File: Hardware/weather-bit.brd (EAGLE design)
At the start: 68.6 x 67.3 mm, 42 parts, among them J2 RJ11, J3 RJ11, U1 BME280, U2 micro:bit

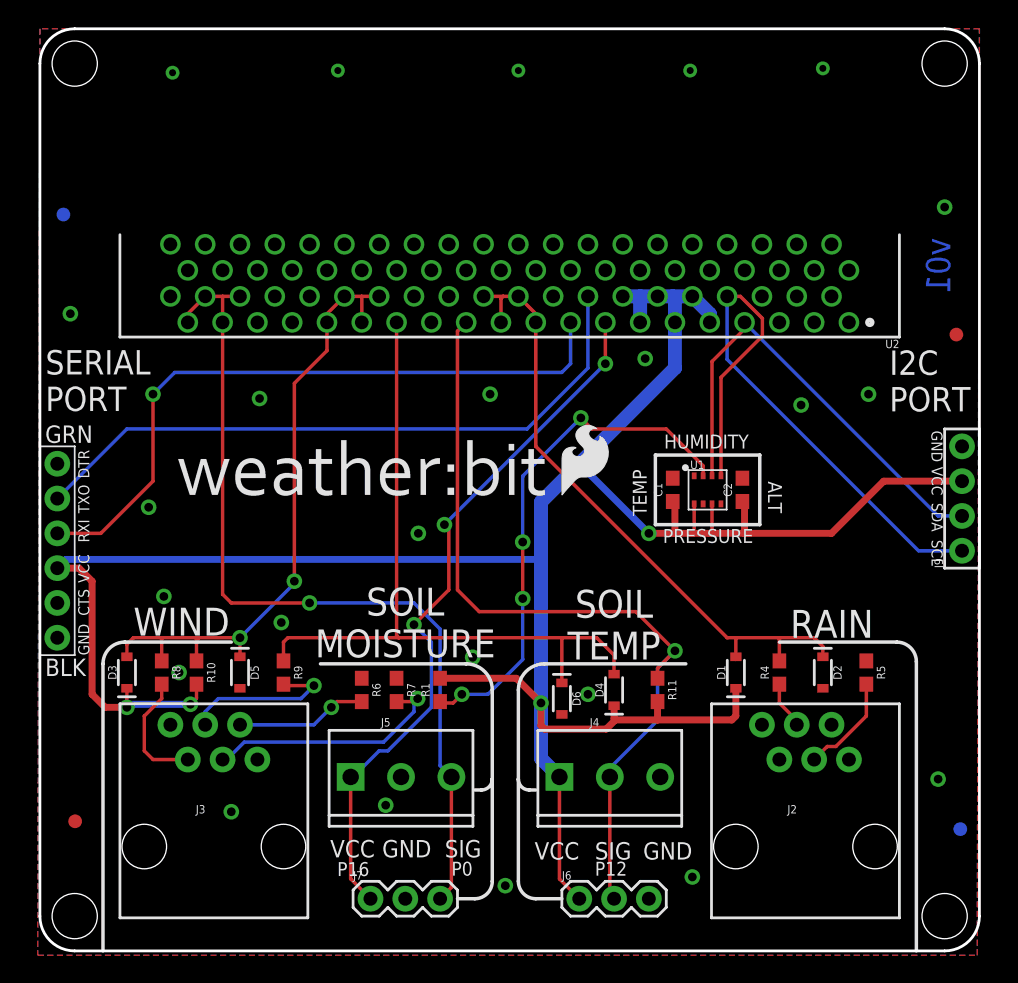
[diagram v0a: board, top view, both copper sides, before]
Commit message: Updated One-Wire Hardware Set-up
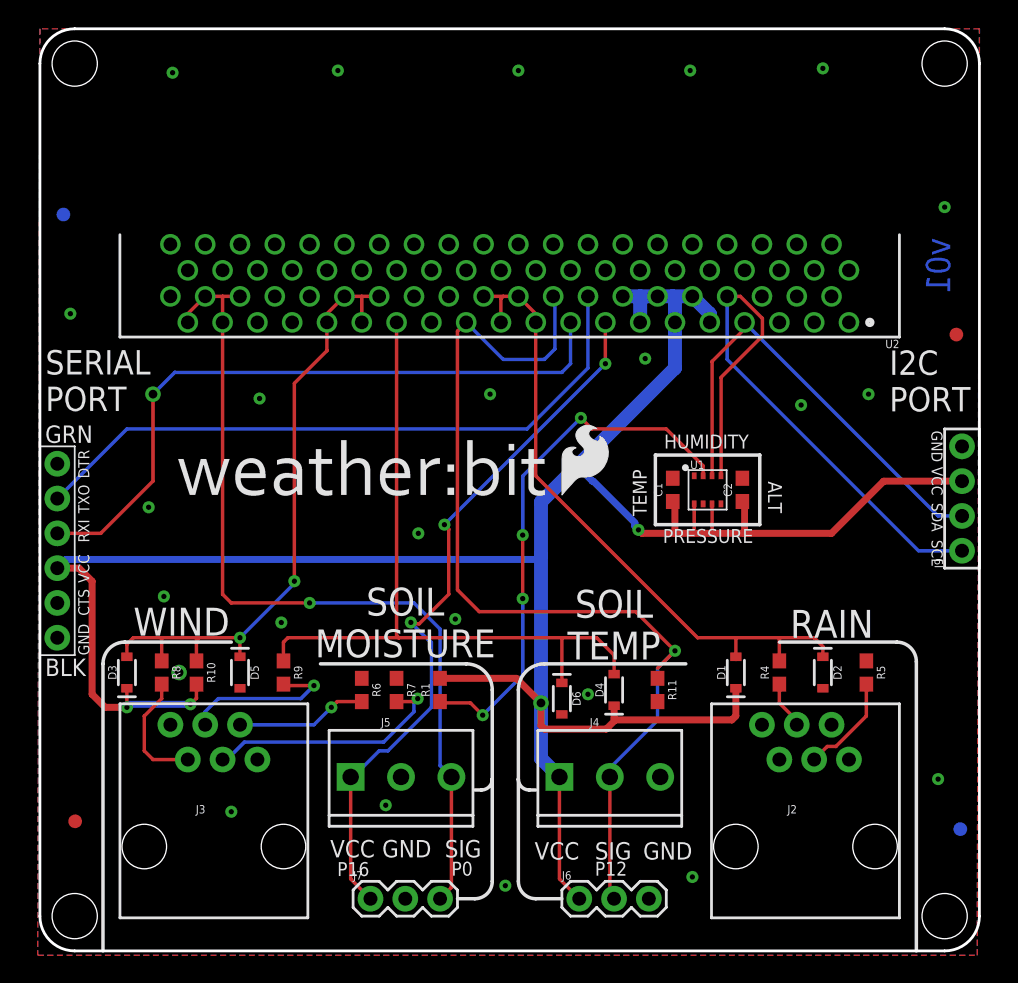
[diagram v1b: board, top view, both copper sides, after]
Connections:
- removed net 13: U2.A18
- net 3.3V: now also R11.1; no longer R11.2
- net TEMP_DAT: now also R11.2, U2.A18; no longer R11.1
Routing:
- net TEMP_DAT: track 60.2 -> 71.4 mm
- net N$2: track 37.9 -> 39.4 mm
- net RAIN: track 47.0 -> 48.3 mm
- net 3.3V: track 186.1 -> 184.9 mm
- net SOIL_PWR: track 52.2 -> 52.9 mm

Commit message: Updating weather:bit per QC review
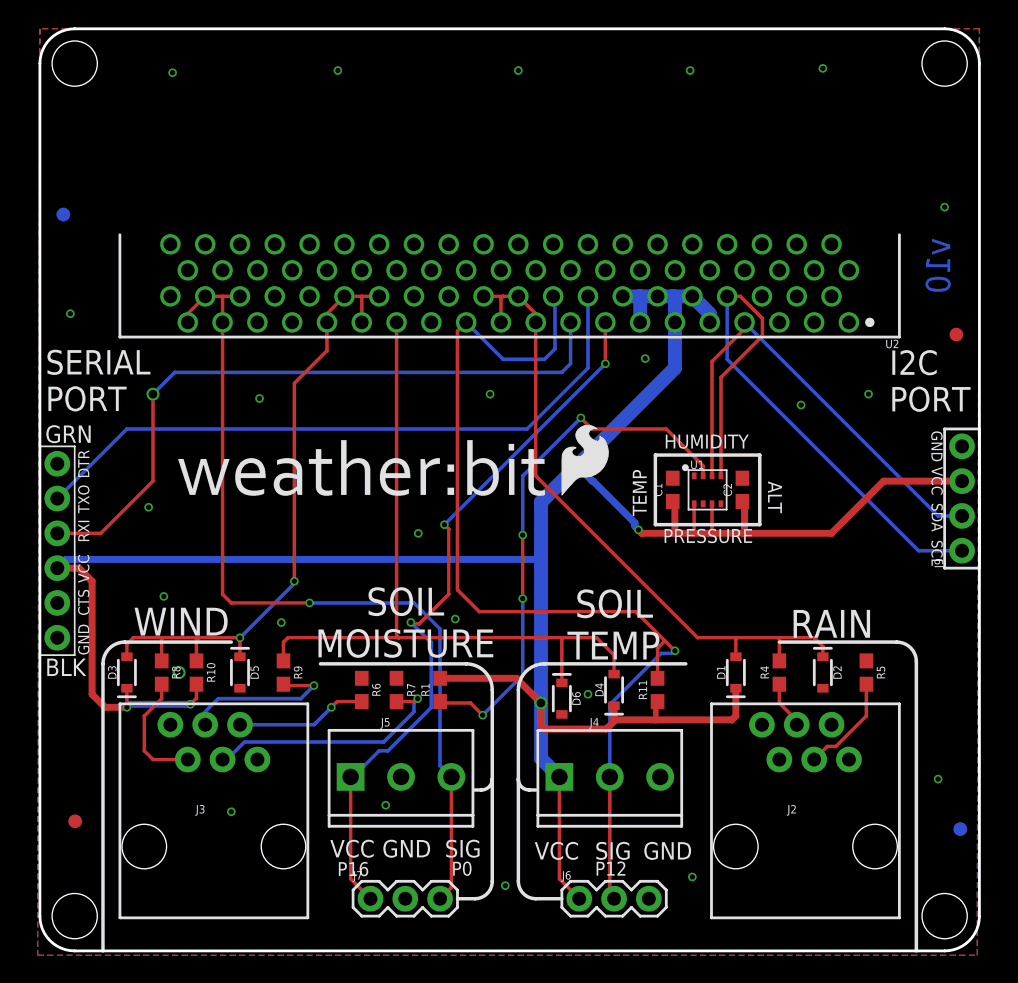
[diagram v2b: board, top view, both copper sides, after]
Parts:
- added U$4: (no value), SparkFun-Aesthetics:ORDERING_INSTRUCTIONS
- turned R11 to 90 degrees
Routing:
- net TEMP_DAT: track 71.4 -> 73.0 mm
- net 3.3V: track 184.9 -> 186.4 mm
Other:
- board text added: "Solder Mask: Black Gloss"
- board text added: "v10"
- board text removed: "v01"
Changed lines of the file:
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@@
 <setting verticaltext="up"/>
 </settings>
-<grid distance="10" unitdist="mil" unit="mil" style="dots" multiple="1" display="yes" altdistance="0.001" altunitdist="mil" altunit="mil"/>
+<grid distance="5" unitdist="mil" unit="mil" style="dots" multiple="1" display="yes" altdistance="0.001" altunitdist="mil" altunit="mil"/>
 <layers>
 <layer number="1" name="Top" color="4" fill="1" visible="yes" active="yes"/>
@@
 <plain>
 <text x="31.75" y="-11.43" size="1.778" layer="51" font="vector" ratio="15">Mary West, based on Weather Shield Design by Nathan Seidle </text>
-<text x="65.56375" y="50.00625" size="1.778" layer="16" font="vector" ratio="15" rot="SMR270" align="center">v01</text>
+<text x="65.56375" y="50.00625" size="1.778" layer="16" font="vector" ratio="15" rot="SMR270" align="center">v10</text>
 <text x="30.63875" y="90.4875" size="1.778" layer="47" font="vector" ratio="15">* All dimensions
   are in inches</text>
@@
 <wire x1="68.58" y1="38.1" x2="68.58" y2="27.94" width="0.2032" layer="21"/>
 <text x="49.022" y="14.605" size="1.778" layer="22" font="vector" ratio="15" rot="MR0">sparkfun.com/microbit</text>
+<text x="6.223" y="-32.385" size="2.54" layer="51">Solder Mask: Black Gloss</text>
 </plain>
 <attributes>
@@
 </class>
 </classes>
-<designrules name="SparkFun-2-layer-STANDARD">
+<designrules name="SparkFun-2-layer-FAB-LIMIT">
 <description language="en">&lt;b&gt;SparkFun 2 Layer Design Rule Checks - STANDARD/TIGHT/FAB-LIMIT&lt;/b&gt;
 &lt;p&gt;
@@
 <param name="mtCopper" value="0.035mm 0.035mm 0.035mm 0.035mm 0.035mm 0.035mm 0.035mm 0.035mm 0.035mm 0.035mm 0.035mm 0.035mm 0.035mm 0.035mm 0.035mm 0.035mm"/>
 <param name="mtIsolate" value="1.5mm 0.15mm 0.2mm 0.15mm 0.2mm 0.15mm 0.2mm 0.15mm 0.2mm 0.15mm 0.2mm 0.15mm 0.2mm 0.15mm 0.2mm"/>
-<param name="mdWireWire" value="10mil"/>
-<param name="mdWirePad" value="8mil"/>
-<param name="mdWireVia" value="10mil"/>
-<param name="mdPadPad" value="8mil"/>
-<param name="mdPadVia" value="10mil"/>
-<param name="mdViaVia" value="10mil"/>
-<param name="mdSmdPad" value="8mil"/>
-<param name="mdSmdVia" value="8mil"/>
-<param name="mdSmdSmd" value="8mil"/>
+<param name="mdWireWire" value="4mil"/>
+<param name="mdWirePad" value="4mil"/>
+<param name="mdWireVia" value="4mil"/>
+<param name="mdPadPad" value="4mil"/>
+<param name="mdPadVia" value="4mil"/>
+<param name="mdViaVia" value="4mil"/>
+<param name="mdSmdPad" value="4mil"/>
+<param name="mdSmdVia" value="4mil"/>
+<param name="mdSmdSmd" value="4mil"/>
 <param name="mdViaViaSameLayer" value="8mil"/>
 <param name="mnLayersViaInSmd" value="2"/>
-<param name="mdCopperDimension" value="8mil"/>
-<param name="mdDrill" value="8mil"/>
+<param name="mdCopperDimension" value="4mil"/>
+<param name="mdDrill" value="4mil"/>
 <param name="mdSmdStop" value="0mil"/>
-<param name="msWidth" value="10mil"/>
-<param name="msDrill" value="20mil"/>
+<param name="msWidth" value="4mil"/>
+<param name="msDrill" value="6mil"/>
 <param name="msMicroVia" value="9.99mm"/>
 <param name="msBlindViaRatio" value="0.5"/>
@@
 <param name="rvMicroViaOuter" value="0.25"/>
 <param name="rvMicroViaInner" value="0.25"/>
-<param name="rlMinPadTop" value="10mil"/>
+<param name="rlMinPadTop" value="5mil"/>
 <param name="rlMaxPadTop" value="20mil"/>
-<param name="rlMinPadInner" value="10mil"/>
+<param name="rlMinPadInner" value="6mil"/>
 <param name="rlMaxPadInner" value="20mil"/>
-<param name="rlMinPadBottom" value="10mil"/>
+<param name="rlMinPadBottom" value="5mil"/>
 <param name="rlMaxPadBottom" value="20mil"/>
-<param name="rlMinViaOuter" value="10mil"/>
+<param name="rlMinViaOuter" value="5mil"/>
 <param name="rlMaxViaOuter" value="20mil"/>
-<param name="rlMinViaInner" value="10mil"/>
+<param name="rlMinViaInner" value="6mil"/>
 <param name="rlMaxViaInner" value="20mil"/>
 <param name="rlMinMicroViaOuter" value="4mil"/>
@@
 <element name="J6" library="SparkFun-Connectors" package="1X03" value="" x="39.37" y="3.81"/>
 <element name="J7" library="SparkFun-Connectors" package="1X03" value="" x="24.13" y="3.81"/>
-<element name="R11" library="SparkFun-Resistors" package="0603" value="4.7k" x="45.085" y="19.05" rot="R270">
-<attribute name="PROD_ID" value="RES-07857" x="45.085" y="19.05" size="1.778" layer="27" rot="R270" display="off"/>
+<element name="R11" library="SparkFun-Resistors" package="0603" value="4.7k" x="45.085" y="19.05" rot="R90">
+<attribute name="PROD_ID" value="RES-07857" x="45.085" y="19.05" size="1.778" layer="27" rot="R90" display="off"/>
 </element>
 <element name="H3" library="SparkFun-Electromechanical" package="STAND-OFF" value="STAND-OFF" x="2.54" y="2.54"/>
@@
 <element name="U$2" library="Micro_Bit_LOGOS" package="LOGO-WEATHERBIT" value="" x="9.907446875" y="33.02"/>
 <element name="U$3" library="Micro_Bit_LOGOS" package="LOGO-WEATHERBIT" value="" x="47.4218" y="25.298396875" rot="MR0"/>
+<element name="U$4" library="SparkFun-Aesthetics" package="ORDERING_INSTRUCTIONS" value="" x="1.143" y="-16.637"/>
 </elements>
 <signals>
@@
 <wire x1="3.81" y1="18.7325" x2="4.7625" y2="17.78" width="0.508" layer="1"/>
 <wire x1="4.7625" y1="17.78" x2="6.35" y2="17.78" width="0.508" layer="1"/>
-<wire x1="42.00525" y1="16.85925" x2="50.51425" y2="16.85925" width="0.508" layer="1"/>
+<wire x1="42.00525" y1="16.85925" x2="44.958" y2="16.85925" width="0.508" layer="1"/>
+<wire x1="44.958" y1="16.85925" x2="50.51425" y2="16.85925" width="0.508" layer="1"/>
 <wire x1="50.51425" y1="16.85925" x2="50.8" y2="17.145" width="0.508" layer="1"/>
 <wire x1="50.8" y1="17.145" x2="50.8" y2="19.17" width="0.508" layer="1"/>
@@
 <wire x1="40.3225" y1="34.29" x2="40.386" y2="34.29" width="0.508" layer="16"/>
 <wire x1="40.386" y1="34.29" x2="43.434" y2="31.242" width="0.508" layer="16"/>
-<wire x1="41.91" y1="17.9" x2="45.085" y2="19.9" width="0" layer="19" extent="1-1"/>
+<wire x1="45.085" y1="18.2" x2="44.958" y2="18.2" width="0.4064" layer="1"/>
+<wire x1="44.958" y1="18.2" x2="44.958" y2="16.85925" width="0.4064" layer="1"/>
 </signal>
 <signal name="N$2">
@@
 <contactref element="J4" pad="2"/>
 <wire x1="41.6" y1="12.7" x2="41.6" y2="4.12" width="0.254" layer="1"/>
-<wire x1="41.6" y1="12.7" x2="41.6" y2="13.3425" width="0.254" layer="16"/>
-<wire x1="41.6" y1="13.3425" x2="45.085" y2="16.8275" width="0.254" layer="16"/>
 <via x="46.355" y="21.9075" extent="1-16" drill="0.381"/>
 <wire x1="32.0675" y1="24.765" x2="43.4975" y2="24.765" width="0.254" layer="1"/>
@@
 <wire x1="30.48" y1="45.24375" x2="31.115" y2="45.87875" width="0.254" layer="1"/>
 <contactref element="J6" pad="2"/>
-<wire x1="43.4975" y1="24.765" x2="46.355" y2="21.9075" width="0.254" layer="1"/>
-<wire x1="45.085" y1="20.6375" x2="46.355" y2="21.9075" width="0.254" layer="1"/>
-<wire x1="45.085" y1="16.8275" x2="45.085" y2="20.6375" width="0.254" layer="16"/>
-<wire x1="45.085" y1="20.6375" x2="46.355" y2="21.9075" width="0.254" layer="16"/>
+<wire x1="43.4975" y1="24.765" x2="45.62475" y2="22.63775" width="0.254" layer="1"/>
+<wire x1="45.62475" y1="22.63775" x2="46.355" y2="21.9075" width="0.254" layer="1"/>
 <wire x1="41.6" y1="4.12" x2="41.91" y2="3.81" width="0.254" layer="1"/>
 <contactref element="R11" pad="2"/>
 <contactref element="U2" pad="A18"/>
-<wire x1="45.085" y1="18.2" x2="45.085" y2="16.8275" width="0" layer="19" extent="1-16"/>
 <wire x1="37.465" y1="47.77875" x2="37.592" y2="47.77875" width="0.254" layer="16"/>
 <wire x1="37.592" y1="47.77875" x2="37.592" y2="43.942" width="0.254" layer="16"/>
@@
 <wire x1="36.83" y1="43.18" x2="33.81375" y2="43.18" width="0.254" layer="16"/>
 <wire x1="33.81375" y1="43.18" x2="31.115" y2="45.87875" width="0.254" layer="16"/>
+<wire x1="41.6" y1="12.7" x2="41.6" y2="17.978" width="0.254" layer="16"/>
+<wire x1="41.6" y1="17.978" x2="45.339" y2="21.717" width="0.254" layer="16"/>
+<wire x1="45.339" y1="21.717" x2="46.1645" y2="21.717" width="0.254" layer="16"/>
+<wire x1="46.1645" y1="21.717" x2="46.355" y2="21.9075" width="0.254" layer="16"/>
+<wire x1="45.085" y1="19.9" x2="45.085" y2="22.098" width="0.254" layer="1"/>
+<wire x1="45.085" y1="22.098" x2="45.62475" y2="22.63775" width="0.254" layer="1"/>
 </signal>
 <signal name="SOIL_PWR">
@@
 </signal>
 </signals>
+<errors>
+</errors>
 </board>
 </drawing>

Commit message: Added qwiic connector and logos
- added vertical qwiic connector near the 4-pin I2C header
- added qwiic logo near connector
- added big qwiic logos near product names on top and bottom silk
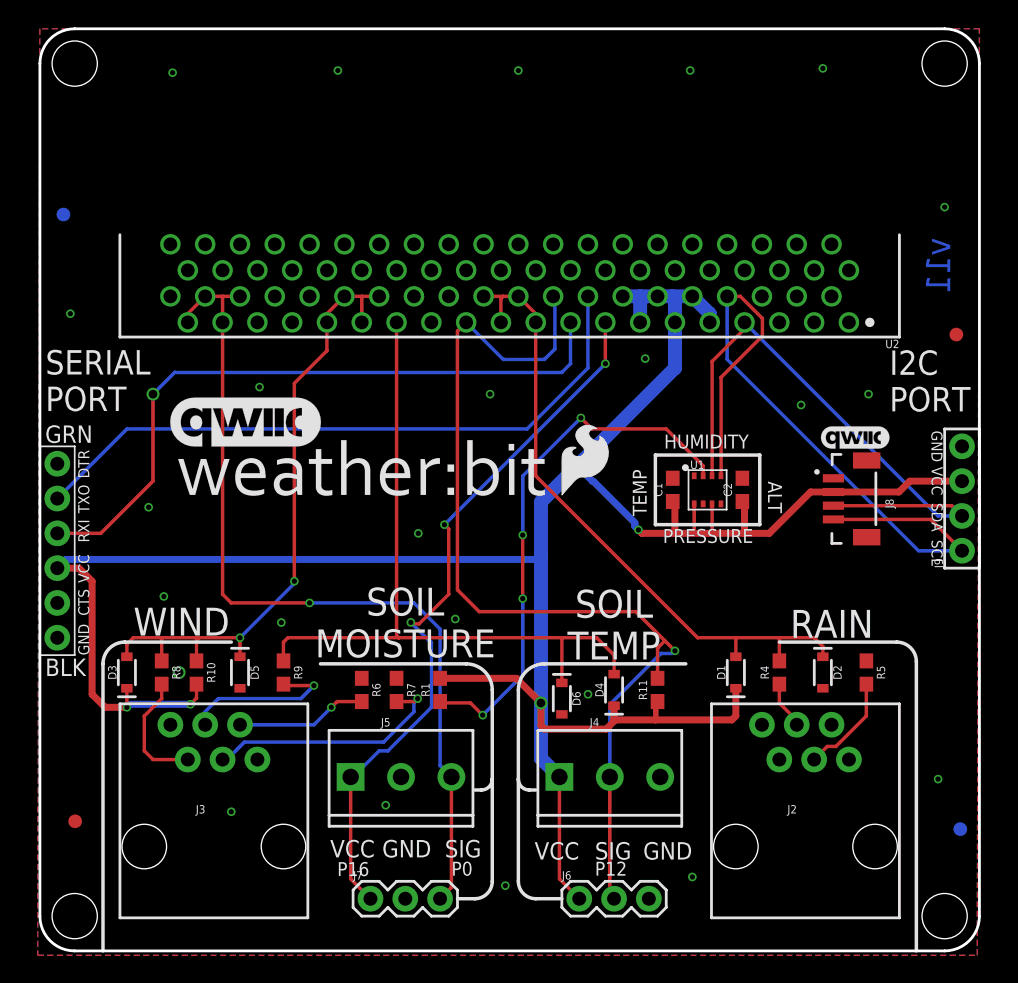
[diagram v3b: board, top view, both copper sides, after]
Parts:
- added J8: Qwiic (vertical), SparkFun-Connectors:JST04_1MM_VERT
- added U$5: (no value), SparkFun-Aesthetics:QWIIC_5MM
- added U$6, U$7: (no value), SparkFun-Aesthetics:QWIIC_11MM
- J9: value (none) -> PTH
- moved U$3 4.98 mm to (42.4, 25.2)
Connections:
- net 3.3V: now also J8.2
- net GND: now also J8.1
- net SCL: now also J8.4
- net SDA: now also J8.3
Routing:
- net SCL: track 43.5 -> 53.8 mm
- net SDA: track 33.9 -> 43.6 mm
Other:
- board text added: "v11"
- board text removed: "v10"

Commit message: SMD connector on 40 pin RA, and 4-pin I2C header
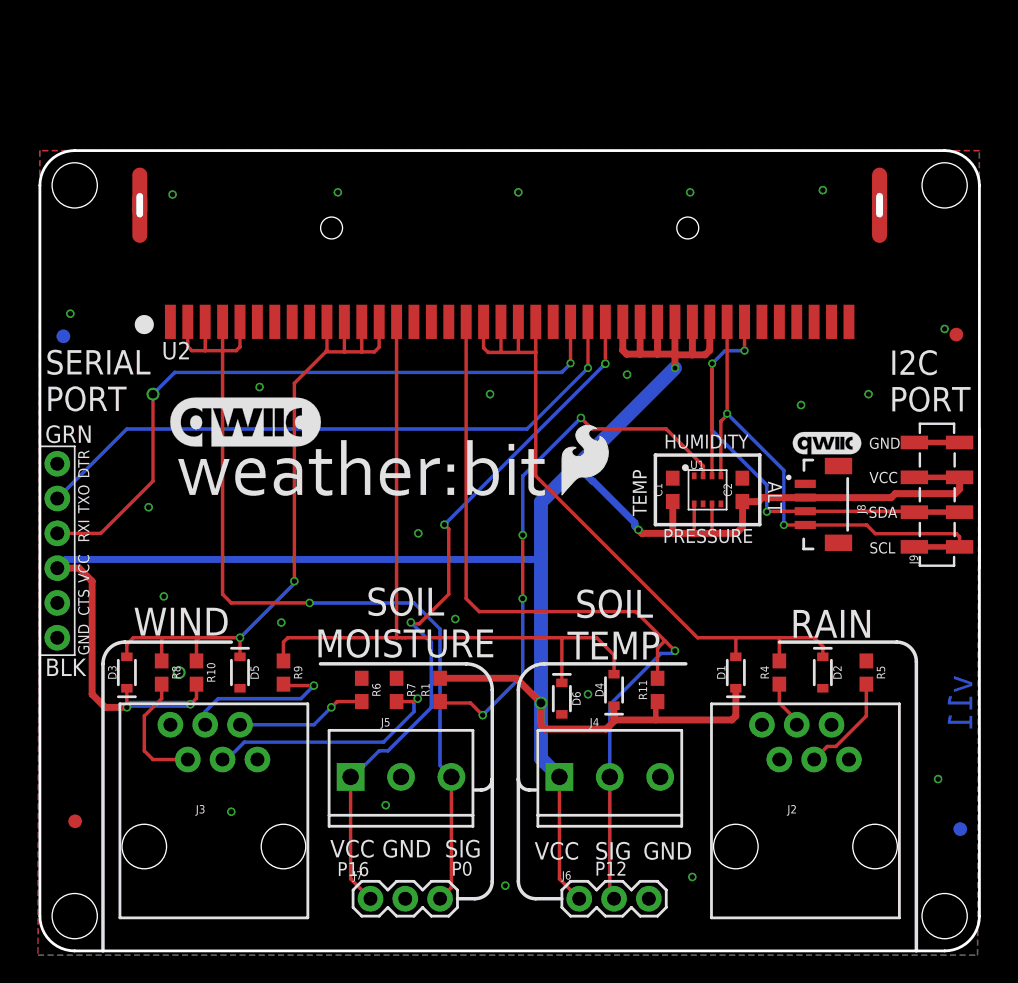
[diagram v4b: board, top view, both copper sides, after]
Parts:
- J6, J7: value (none) -> 455-1750-1-ND
- J9: value PTH -> 1X04_SMD_STRAIGHT_COMBO; device SparkFun-Connectors:1X04_NO_SILK -> SparkFun-Connectors:1X04_SMD_VERTICAL_COMBO
- U2: device Micro_Bit_Parts:MICRO:BIT_RA_PTH -> SparkFun-Connectors:MICRO:BIT-RA_SMD
- moved FD3 8.89 mm to (1.71, 44.9)
- moved H1 8.89 mm to (2.54, 55.9)
- moved H2 8.89 mm to (66.0, 55.9)
- moved J8 2.10 mm to (55.1, 32.6)
- moved U$5 2.10 mm to (57.4, 37.1)
- moved J9 1.85 mm to (65.5, 29.5)
- moved U2 1.43 mm to (34.3, 52.1), turned to 0 degrees
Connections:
- new net N$3: U2.P$23
- net 10: now also U2.P$16; no longer U2.A25
- net 11: now also U2.P$17; no longer U2.A24
- net 3: now also U2.P$1; no longer U2.A40
- net 3.3V: now also U2.P$27, U2.P$28, U2.P$29, U2.P$30, U2.P$31, U2.P$32; no longer U2.A10, U2.A11, U2.A12, U2.A13, U2.A14, U2.A9
- net 4: now also U2.P$6; no longer U2.A35
- net 5: now also U2.P$7; no longer U2.A34
- net 6: now also U2.P$8; no longer U2.A33
- net 7: now also U2.P$9; no longer U2.A32
- net 9: now also U2.P$15; no longer U2.A26
- net GND: now also U2.P$35, U2.P$36, U2.P$37, U2.P$38, U2.P$39, U2.P$40; no longer U2.A1, U2.A2, U2.A3, U2.A4, U2.A5, U2.A6
- net RAIN: now also U2.P$19, U2.P$20, U2.P$21, U2.P$22; no longer U2.A19, U2.A20, U2.A21, U2.A22
- net RXI: now also U2.P$24; no longer U2.A17
- net SCL: now also U2.P$33; no longer U2.A8
- net SDA: now also U2.P$34; no longer U2.A7
- net SOIL_DAT: now also U2.P$2, U2.P$3, U2.P$4, U2.P$5; no longer U2.A36, U2.A37, U2.A38, U2.A39
- net SOIL_PWR: now also U2.P$26; no longer U2.A15
- net TEMP_DAT: now also U2.P$18; no longer U2.A18, U2.A23
- net TXO: now also U2.P$25; no longer U2.A16
- net WDIR: now also U2.P$10, U2.P$11, U2.P$12, U2.P$13; no longer U2.A28, U2.A29, U2.A30, U2.A31
- net WSPEED: now also U2.P$14; no longer U2.A27
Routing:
- net SCL: track 53.8 -> 35.2 mm, vias 0 -> 2
- net TEMP_DAT: track 73.0 -> 60.7 mm
- net SDA: track 43.6 -> 36.4 mm, vias 0 -> 3
- net 3.3V: track 186.4 -> 191.9 mm, vias 4 -> 5
- net WDIR: track 46.7 -> 50.2 mm
- net RAIN: track 48.3 -> 51.7 mm
- net SOIL_DAT: track 64.0 -> 67.0 mm
- net TXO: track 47.9 -> 46.1 mm, vias 0 -> 1
- net RXI: track 49.3 -> 49.4 mm, vias 1 -> 2
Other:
- board size 68.6 x 67.3 mm -> 68.6 x 58.4 mm
